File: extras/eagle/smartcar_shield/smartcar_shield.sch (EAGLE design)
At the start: 21 parts, among them IC1 L293D, J1 ARDUINO_R3_SHIELD

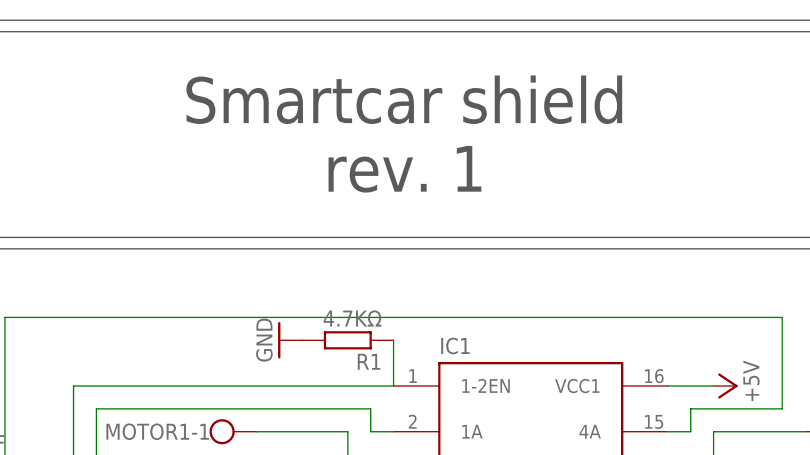
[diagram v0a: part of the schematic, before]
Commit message: Update board to rev. 2
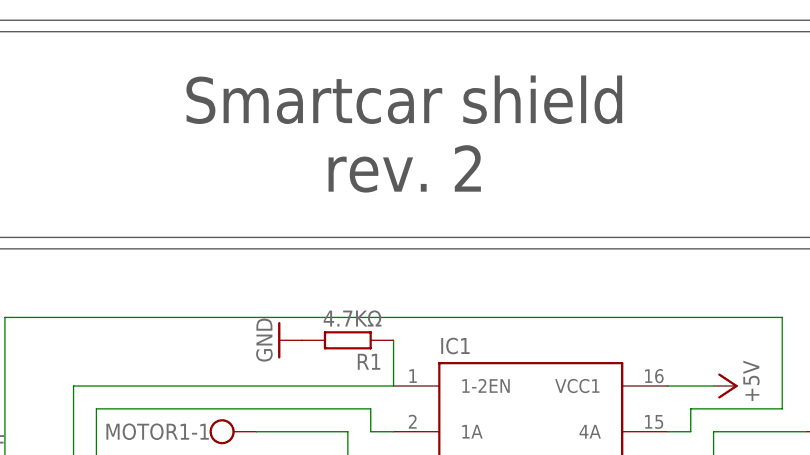
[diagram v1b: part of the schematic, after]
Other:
- note added: "Smartcar shield rev. 2"
- note removed: "Smartcar shield rev. 1"
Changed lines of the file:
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@@
 <?xml version="1.0" encoding="utf-8"?>
 <!DOCTYPE eagle SYSTEM "eagle.dtd">
-<eagle version="7.5.0">
+<eagle version="8.7.1">
 <drawing>
 <settings>
 <setting alwaysvectorfont="no"/>
+<setting keepoldvectorfont="yes"/>
 <setting verticaltext="up"/>
 </settings>
-<grid distance="0.05" unitdist="inch" unit="inch" style="lines" multiple="1" display="no" altdistance="0.01" altunitdist="inch" altunit="inch"/>
+<grid distance="0.1" unitdist="inch" unit="inch" style="lines" multiple="1" display="no" altdistance="0.01" altunitdist="inch" altunit="inch"/>
 <layers>
 <layer number="1" name="Top" color="4" fill="1" visible="no" active="no"/>
@@
 <layer number="112" name="tSilk" color="7" fill="1" visible="no" active="yes"/>
 <layer number="113" name="IDFDebug" color="4" fill="1" visible="no" active="yes"/>
+<layer number="114" name="FRNTMAAT1" color="7" fill="1" visible="no" active="no"/>
+<layer number="115" name="FRNTMAAT2" color="7" fill="1" visible="no" active="no"/>
 <layer number="116" name="Patch_BOT" color="9" fill="4" visible="no" active="yes"/>
+<layer number="117" name="BACKMAAT1" color="7" fill="1" visible="no" active="no"/>
 <layer number="118" name="Rect_Pads" color="7" fill="1" visible="yes" active="yes"/>
+<layer number="119" name="KAP_TEKEN" color="7" fill="1" visible="no" active="no"/>
+<layer number="120" name="KAP_MAAT1" color="7" fill="1" visible="no" active="no"/>
 <layer number="121" name="_tsilk" color="7" fill="1" visible="no" active="yes"/>
 <layer number="122" name="_bsilk" color="7" fill="1" visible="no" active="yes"/>
@@
 <layer number="128" name="_bValues" color="7" fill="1" visible="no" active="yes"/>
 <layer number="129" name="Mask" color="7" fill="1" visible="yes" active="yes"/>
+<layer number="130" name="SMDSTROOK" color="7" fill="1" visible="no" active="no"/>
 <layer number="131" name="tAdjust" color="7" fill="1" visible="no" active="yes"/>
 <layer number="132" name="bAdjust" color="7" fill="1" visible="no" active="yes"/>
+<layer number="133" name="bottom_silk" color="7" fill="1" visible="no" active="no"/>
 <layer number="144" name="Drill_legend" color="7" fill="1" visible="no" active="yes"/>
 <layer number="150" name="Notes" color="7" fill="1" visible="no" active="yes"/>
@@
 <layer number="230" name="230bmp" color="7" fill="1" visible="yes" active="yes"/>
 <layer number="231" name="231bmp" color="7" fill="1" visible="yes" active="yes"/>
+<layer number="232" name="Eagle3D_PG2" color="7" fill="1" visible="no" active="no"/>
+<layer number="233" name="Eagle3D_PG3" color="7" fill="1" visible="no" active="no"/>
 <layer number="248" name="Housing" color="7" fill="1" visible="no" active="yes"/>
 <layer number="249" name="Edge" color="7" fill="1" visible="no" active="yes"/>
@@
 <wire x1="175.26" y1="125.73" x2="175.26" y2="148.59" width="0.1524" layer="97"/>
 <text x="229.87" y="130.81" size="5.08" layer="97" align="bottom-center">Smartcar shield
-rev. 1</text>
+rev. 2</text>
 <wire x1="128.27" y1="60.96" x2="184.15" y2="60.96" width="0.1524" layer="97"/>
 <wire x1="184.15" y1="60.96" x2="184.15" y2="29.21" width="0.1524" layer="97"/>
